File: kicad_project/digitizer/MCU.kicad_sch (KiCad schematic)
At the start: 27 parts, among them J401 SHF-105-01-L-D-TH-TR, U401 ATSAM4E8EA-AN

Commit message: updated schematic to use all 0805 parts (both caps and resistors)
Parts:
- C401, C403, C404, C405, C406, C407, C408, C409, C410, C411, C412, C413, C414, C415, C416: footprint Capacitor_SMD:C_2220_5650Metric_Pad1.97x5.40mm_HandSolder -> Capacitor_SMD:C_0805_2012Metric_Pad1.18x1.45mm_HandSolder
- C402: footprint Capacitor_Tantalum_SMD:CP_EIA-6032-20_AVX-F_Pad2.25x2.35mm_HandSolder -> Capacitor_SMD:C_0805_2012Metric_Pad1.18x1.45mm_HandSolder
- R401, R402, R403, R404, R405, R406, R407: footprint Resistor_SMD:R_2512_6332Metric_Pad1.40x3.35mm_HandSolder -> Resistor_SMD:R_0805_2012Metric_Pad1.20x1.40mm_HandSolder
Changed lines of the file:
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@@
       (effects (font (size 1.27 1.27)) (justify left))
     )
-    (property "Footprint" "Resistor_SMD:R_2512_6332Metric_Pad1.40x3.35mm_HandSolder" (id 2) (at 66.04 90.17 0)
+    (property "Footprint" "Resistor_SMD:R_0805_2012Metric_Pad1.20x1.40mm_HandSolder" (id 2) (at 66.04 90.17 0)
       (effects (font (size 1.27 1.27)) hide)
     )
@@
       (effects (font (size 1.27 1.27)) (justify left))
     )
-    (property "Footprint" "Capacitor_SMD:C_2220_5650Metric_Pad1.97x5.40mm_HandSolder" (id 2) (at 243.84 52.07 0)
+    (property "Footprint" "Capacitor_SMD:C_0805_2012Metric_Pad1.18x1.45mm_HandSolder" (id 2) (at 243.84 52.07 0)
       (effects (font (size 1.27 1.27)) hide)
     )
@@
       (effects (font (size 1.27 1.27)) (justify left))
     )
-    (property "Footprint" "Resistor_SMD:R_2512_6332Metric_Pad1.40x3.35mm_HandSolder" (id 2) (at 49.53 132.08 0)
+    (property "Footprint" "Resistor_SMD:R_0805_2012Metric_Pad1.20x1.40mm_HandSolder" (id 2) (at 49.53 132.08 0)
       (effects (font (size 1.27 1.27)) hide)
     )
@@
       (effects (font (size 1.27 1.27)) (justify left))
     )
-    (property "Footprint" "Resistor_SMD:R_2512_6332Metric_Pad1.40x3.35mm_HandSolder" (id 2) (at 151.13 78.74 0)
+    (property "Footprint" "Resistor_SMD:R_0805_2012Metric_Pad1.20x1.40mm_HandSolder" (id 2) (at 151.13 78.74 0)
       (effects (font (size 1.27 1.27)) hide)
     )
@@
       (effects (font (size 1.27 1.27)) (justify left))
     )
-    (property "Footprint" "Capacitor_SMD:C_2220_5650Metric_Pad1.97x5.40mm_HandSolder" (id 2) (at 238.76 146.05 0)
+    (property "Footprint" "Capacitor_SMD:C_0805_2012Metric_Pad1.18x1.45mm_HandSolder" (id 2) (at 238.76 146.05 0)
       (effects (font (size 1.27 1.27)) hide)
     )
@@
       (effects (font (size 1.27 1.27)) (justify left))
     )
-    (property "Footprint" "Capacitor_SMD:C_2220_5650Metric_Pad1.97x5.40mm_HandSolder" (id 2) (at 246.38 146.05 0)
+    (property "Footprint" "Capacitor_SMD:C_0805_2012Metric_Pad1.18x1.45mm_HandSolder" (id 2) (at 246.38 146.05 0)
       (effects (font (size 1.27 1.27)) hide)
     )
@@
       (effects (font (size 1.27 1.27)) (justify left))
     )
-    (property "Footprint" "Capacitor_Tantalum_SMD:CP_EIA-6032-20_AVX-F_Pad2.25x2.35mm_HandSolder" (id 2) (at 237.49 34.29 0)
+    (property "Footprint" "Capacitor_SMD:C_0805_2012Metric_Pad1.18x1.45mm_HandSolder" (id 2) (at 237.49 34.29 0)
       (effects (font (size 1.27 1.27)) hide)
     )
@@
       (effects (font (size 1.27 1.27)) (justify left))
     )
-    (property "Footprint" "Capacitor_SMD:C_2220_5650Metric_Pad1.97x5.40mm_HandSolder" (id 2) (at 213.36 146.05 0)
+    (property "Footprint" "Capacitor_SMD:C_0805_2012Metric_Pad1.18x1.45mm_HandSolder" (id 2) (at 213.36 146.05 0)
       (effects (font (size 1.27 1.27)) hide)
     )
@@
       (effects (font (size 1.27 1.27)) (justify left))
     )
-    (property "Footprint" "Capacitor_SMD:C_2220_5650Metric_Pad1.97x5.40mm_HandSolder" (id 2) (at 254 146.05 0)
+    (property "Footprint" "Capacitor_SMD:C_0805_2012Metric_Pad1.18x1.45mm_HandSolder" (id 2) (at 254 146.05 0)
       (effects (font (size 1.27 1.27)) hide)
     )
@@
       (effects (font (size 1.27 1.27)) (justify left))
     )
-    (property "Footprint" "Capacitor_SMD:C_2220_5650Metric_Pad1.97x5.40mm_HandSolder" (id 2) (at 62.23 146.05 0)
+    (property "Footprint" "Capacitor_SMD:C_0805_2012Metric_Pad1.18x1.45mm_HandSolder" (id 2) (at 62.23 146.05 0)
       (effects (font (size 1.27 1.27)) hide)
     )
@@
       (effects (font (size 1.27 1.27)) (justify left))
     )
-    (property "Footprint" "Resistor_SMD:R_2512_6332Metric_Pad1.40x3.35mm_HandSolder" (id 2) (at 58.42 74.93 0)
+    (property "Footprint" "Resistor_SMD:R_0805_2012Metric_Pad1.20x1.40mm_HandSolder" (id 2) (at 58.42 74.93 0)
       (effects (font (size 1.27 1.27)) hide)
     )
@@
       (effects (font (size 1.27 1.27)) (justify left))
     )
-    (property "Footprint" "Resistor_SMD:R_2512_6332Metric_Pad1.40x3.35mm_HandSolder" (id 2) (at 62.23 82.55 0)
+    (property "Footprint" "Resistor_SMD:R_0805_2012Metric_Pad1.20x1.40mm_HandSolder" (id 2) (at 62.23 82.55 0)
       (effects (font (size 1.27 1.27)) hide)
     )
@@
       (effects (font (size 1.27 1.27)) (justify left))
     )
-    (property "Footprint" "Capacitor_SMD:C_2220_5650Metric_Pad1.97x5.40mm_HandSolder" (id 2) (at 198.12 146.05 0)
+    (property "Footprint" "Capacitor_SMD:C_0805_2012Metric_Pad1.18x1.45mm_HandSolder" (id 2) (at 198.12 146.05 0)
       (effects (font (size 1.27 1.27)) hide)
     )
@@
       (effects (font (size 1.27 1.27)) (justify left))
     )
-    (property "Footprint" "Capacitor_SMD:C_2220_5650Metric_Pad1.97x5.40mm_HandSolder" (id 2) (at 243.84 34.29 0)
+    (property "Footprint" "Capacitor_SMD:C_0805_2012Metric_Pad1.18x1.45mm_HandSolder" (id 2) (at 243.84 34.29 0)
       (effects (font (size 1.27 1.27)) hide)
     )
@@
       (effects (font (size 1.27 1.27)) (justify left))
     )
-    (property "Footprint" "Capacitor_SMD:C_2220_5650Metric_Pad1.97x5.40mm_HandSolder" (id 2) (at 269.24 146.05 0)
+    (property "Footprint" "Capacitor_SMD:C_0805_2012Metric_Pad1.18x1.45mm_HandSolder" (id 2) (at 269.24 146.05 0)
       (effects (font (size 1.27 1.27)) hide)
     )
@@
       (effects (font (size 1.27 1.27)) (justify left))
     )
-    (property "Footprint" "Capacitor_SMD:C_2220_5650Metric_Pad1.97x5.40mm_HandSolder" (id 2) (at 276.86 146.05 0)
+    (property "Footprint" "Capacitor_SMD:C_0805_2012Metric_Pad1.18x1.45mm_HandSolder" (id 2) (at 276.86 146.05 0)
       (effects (font (size 1.27 1.27)) hide)
     )
@@
       (effects (font (size 1.27 1.27)) (justify left))
     )
-    (property "Footprint" "Capacitor_SMD:C_2220_5650Metric_Pad1.97x5.40mm_HandSolder" (id 2) (at 243.84 21.59 0)
+    (property "Footprint" "Capacitor_SMD:C_0805_2012Metric_Pad1.18x1.45mm_HandSolder" (id 2) (at 243.84 21.59 0)
       (effects (font (size 1.27 1.27)) hide)
     )
@@
       (effects (font (size 1.27 1.27)) (justify left))
     )
-    (property "Footprint" "Capacitor_SMD:C_2220_5650Metric_Pad1.97x5.40mm_HandSolder" (id 2) (at 261.62 146.05 0)
+    (property "Footprint" "Capacitor_SMD:C_0805_2012Metric_Pad1.18x1.45mm_HandSolder" (id 2) (at 261.62 146.05 0)
       (effects (font (size 1.27 1.27)) hide)
     )
@@
       (effects (font (size 1.27 1.27)) (justify left))
     )
-    (property "Footprint" "Capacitor_SMD:C_2220_5650Metric_Pad1.97x5.40mm_HandSolder" (id 2) (at 228.6 146.05 0)
+    (property "Footprint" "Capacitor_SMD:C_0805_2012Metric_Pad1.18x1.45mm_HandSolder" (id 2) (at 228.6 146.05 0)
       (effects (font (size 1.27 1.27)) hide)
     )
@@
       (effects (font (size 1.27 1.27)) (justify left))
     )
-    (property "Footprint" "Capacitor_SMD:C_2220_5650Metric_Pad1.97x5.40mm_HandSolder" (id 2) (at 220.98 146.05 0)
+    (property "Footprint" "Capacitor_SMD:C_0805_2012Metric_Pad1.18x1.45mm_HandSolder" (id 2) (at 220.98 146.05 0)
       (effects (font (size 1.27 1.27)) hide)
     )
@@
       (effects (font (size 1.27 1.27)) (justify left))
     )
-    (property "Footprint" "Resistor_SMD:R_2512_6332Metric_Pad1.40x3.35mm_HandSolder" (id 2) (at 147.32 78.74 0)
+    (property "Footprint" "Resistor_SMD:R_0805_2012Metric_Pad1.20x1.40mm_HandSolder" (id 2) (at 147.32 78.74 0)
       (effects (font (size 1.27 1.27)) hide)
     )
@@
       (effects (font (size 1.27 1.27)) (justify left))
     )
-    (property "Footprint" "Capacitor_SMD:C_2220_5650Metric_Pad1.97x5.40mm_HandSolder" (id 2) (at 205.74 146.05 0)
+    (property "Footprint" "Capacitor_SMD:C_0805_2012Metric_Pad1.18x1.45mm_HandSolder" (id 2) (at 205.74 146.05 0)
       (effects (font (size 1.27 1.27)) hide)
     )
@@
       (effects (font (size 1.27 1.27)) (justify left))
     )
-    (property "Footprint" "Resistor_SMD:R_2512_6332Metric_Pad1.40x3.35mm_HandSolder" (id 2) (at 54.61 68.58 0)
-      (effects (font (size 1.27 1.27)) hide)
-    )
+    (property "Footprint" "Resistor_SMD:R_0805_2012Metric_Pad1.20x1.40mm_HandSolder" (id 2) (at 54.61 68.58 0)
+      (effects (font (size 1.27 1.27)) hide)
+    )

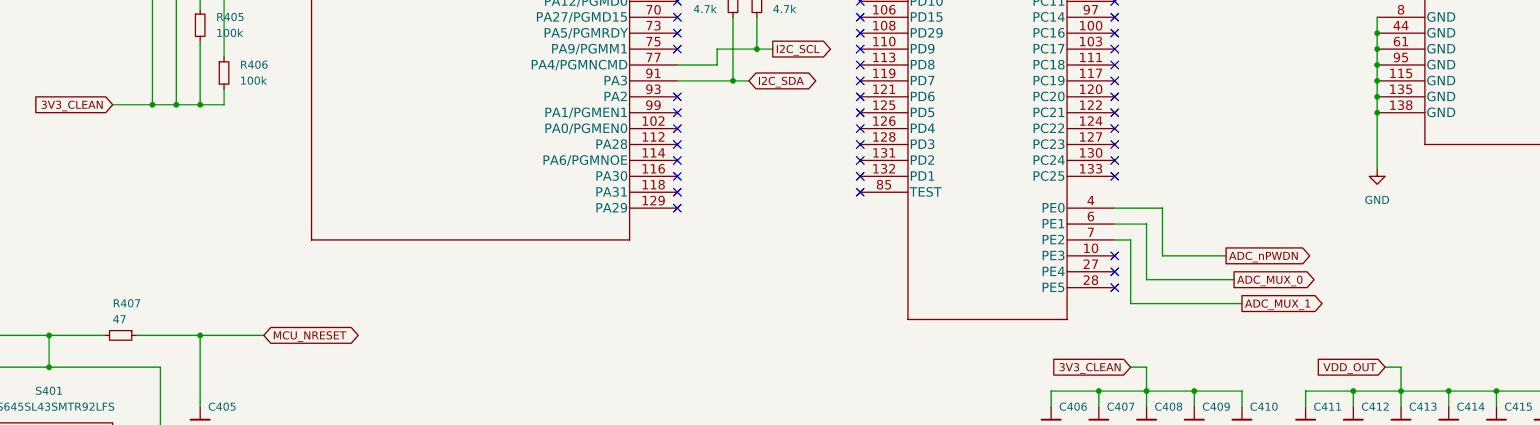
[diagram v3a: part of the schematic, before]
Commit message: added some 0R resistors to pads to allow for easier board modding
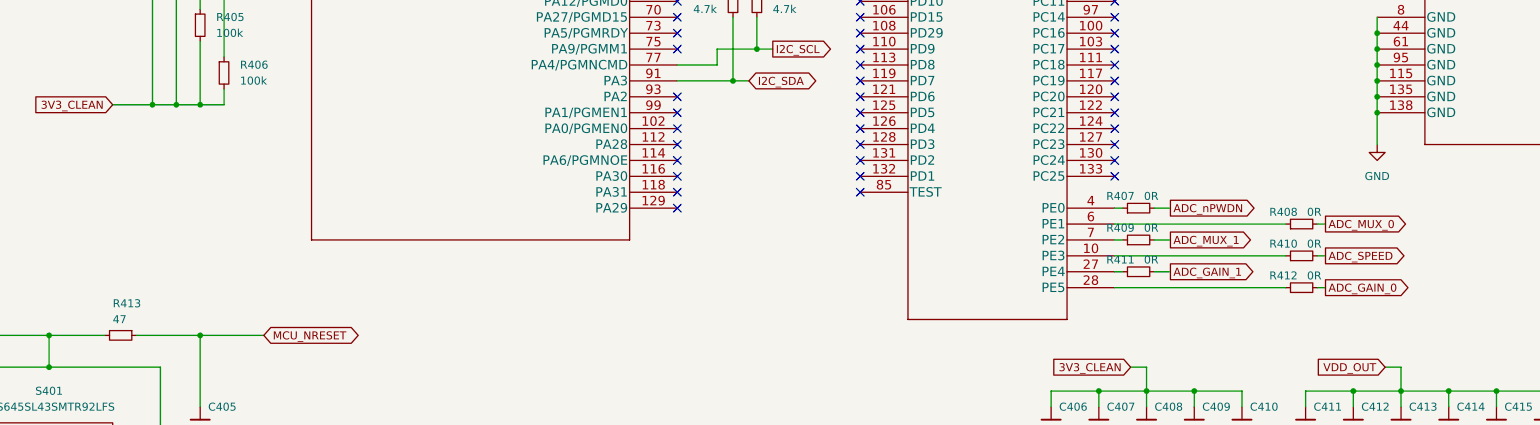
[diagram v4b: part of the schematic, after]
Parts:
- added R407, R408, R409, R410, R411, R412: 0R, Resistor_SMD:R_0805_2012Metric_Pad1.20x1.40mm_HandSolder, symbol Device:R_Small
- renumbered R407 to R413
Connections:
- net ADC_MUX_0: now also R408.2; no longer U401.6 (PE1)
- net ADC_MUX_1: now also R409.2; no longer U401.7 (PE2)
- net ADC_nPWDN: now also R407.2; no longer U401.4 (PE0)
- net at U401.10 (PE3): now also R410.1
- net at U401.27 (PE4): now also R411.1
- net at U401.28 (PE5): now also R412.1
- new net: R407.1, U401.4 (PE0)
- new net: R408.1, U401.6 (PE1)
- new net: R409.1, U401.7 (PE2)
- new net ADC_GAIN_0: R412.2
- new net ADC_GAIN_1: R411.2
- new net ADC_SPEED: R410.2
- no-connect marks 107 -> 104

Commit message: fixed everything up
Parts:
- removed R407, R408, R409, R410, R411, R412: 0R, Resistor_SMD:R_0805_2012Metric_Pad1.20x1.40mm_HandSolder, symbol Device:R_Small
- renumbered R413 to R407
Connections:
- net ADC_GAIN_0: now also U401.28 (PE5)
- net ADC_GAIN_1: now also U401.27 (PE4)
- net ADC_MUX_0: now also U401.6 (PE1)
- net ADC_MUX_1: now also U401.7 (PE2)
- net ADC_SPEED: now also U401.10 (PE3)
- net ADC_nPWDN: now also U401.4 (PE0)
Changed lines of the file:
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@@
     (stroke (width 0) (type default) (color 0 0 0 0))
   )
-  (wire (pts (xy 240.665 119.38) (xy 241.935 119.38))
-    (stroke (width 0) (type default) (color 0 0 0 0))
-  )
-  (wire (pts (xy 214.63 121.92) (xy 217.17 121.92))
+  (wire (pts (xy 208.28 121.92) (xy 217.17 121.92))
     (stroke (width 0) (type default) (color 0 0 0 0))
   )
@@
     (stroke (width 0) (type default) (color 0 0 0 0))
   )
-  (wire (pts (xy 209.55 116.84) (xy 208.28 116.84))
+  (wire (pts (xy 208.28 116.84) (xy 217.17 116.84))
     (stroke (width 0) (type default) (color 0 0 0 0))
   )
@@
     (stroke (width 0) (type default) (color 0 0 0 0))
   )
-  (wire (pts (xy 214.63 116.84) (xy 217.17 116.84))
-    (stroke (width 0) (type default) (color 0 0 0 0))
-  )
   (wire (pts (xy 243.84 38.1) (xy 243.84 39.37))
     (stroke (width 0) (type default) (color 0 0 0 0))
@@
     (stroke (width 0) (type default) (color 0 0 0 0))
   )
-  (wire (pts (xy 240.665 114.3) (xy 241.935 114.3))
-    (stroke (width 0) (type default) (color 0 0 0 0))
-  )
   (wire (pts (xy 237.49 30.48) (xy 237.49 31.75))
     (stroke (width 0) (type default) (color 0 0 0 0))
@@
     (stroke (width 0) (type default) (color 0 0 0 0))
   )
-  (wire (pts (xy 209.55 111.76) (xy 208.28 111.76))
-    (stroke (width 0) (type default) (color 0 0 0 0))
-  )
   (wire (pts (xy 246.38 140.97) (xy 246.38 143.51))
     (stroke (width 0) (type default) (color 0 0 0 0))
@@
     (stroke (width 0) (type default) (color 0 0 0 0))
   )
-  (wire (pts (xy 208.28 119.38) (xy 235.585 119.38))
+  (wire (pts (xy 208.28 119.38) (xy 241.935 119.38))
     (stroke (width 0) (type default) (color 0 0 0 0))
   )
@@
     (stroke (width 0) (type default) (color 0 0 0 0))
   )
-  (wire (pts (xy 208.28 114.3) (xy 235.585 114.3))
+  (wire (pts (xy 208.28 114.3) (xy 241.935 114.3))
     (stroke (width 0) (type default) (color 0 0 0 0))
   )
@@
     (stroke (width 0) (type default) (color 0 0 0 0))
   )
-  (wire (pts (xy 240.665 124.46) (xy 241.935 124.46))
-    (stroke (width 0) (type default) (color 0 0 0 0))
-  )
   (wire (pts (xy 243.84 30.48) (xy 250.19 30.48))
     (stroke (width 0) (type default) (color 0 0 0 0))
@@
     (stroke (width 0) (type default) (color 0 0 0 0))
   )
-  (wire (pts (xy 208.28 121.92) (xy 209.55 121.92))
-    (stroke (width 0) (type default) (color 0 0 0 0))
-  )
   (wire (pts (xy 151.13 73.66) (xy 151.13 76.2))
     (stroke (width 0) (type default) (color 0 0 0 0))
@@
     (stroke (width 0) (type default) (color 0 0 0 0))
   )
-  (wire (pts (xy 208.28 124.46) (xy 235.585 124.46))
+  (wire (pts (xy 208.28 124.46) (xy 241.935 124.46))
     (stroke (width 0) (type default) (color 0 0 0 0))
   )
@@
     (stroke (width 0) (type default) (color 0 0 0 0))
   )
-  (wire (pts (xy 214.63 111.76) (xy 217.17 111.76))
+  (wire (pts (xy 208.28 111.76) (xy 217.17 111.76))
     (stroke (width 0) (type default) (color 0 0 0 0))
   )
@@
     )
     (pin "1")
-  )
-  (symbol (lib_id "Device:R_Small") (at 212.09 121.92 90) (unit 1)
-    (in_bom yes) (on_board yes)
-    (property "Reference" "R411" (id 0) (at 211.455 120.015 90)
-      (effects (font (size 1.27 1.27)) (justify left))
-    )
-    (property "Value" "0R" (id 1) (at 215.265 120.015 90)
-      (effects (font (size 1.27 1.27)) (justify left))
-    )
-    (property "Footprint" "Resistor_SMD:R_0805_2012Metric_Pad1.20x1.40mm_HandSolder" (id 2) (at 212.09 121.92 0)
-      (effects (font (size 1.27 1.27)) hide)
-    )
-    (property "Datasheet" "~" (id 3) (at 212.09 121.92 0)
-      (effects (font (size 1.27 1.27)) hide)
-    )
-    (pin "1")
-    (pin "2")
-  )
-  (symbol (lib_id "Device:R_Small") (at 212.09 111.76 90) (unit 1)
-    (in_bom yes) (on_board yes)
-    (property "Reference" "R407" (id 0) (at 211.455 109.855 90)
-      (effects (font (size 1.27 1.27)) (justify left))
-    )
-    (property "Value" "0R" (id 1) (at 215.265 109.855 90)
-      (effects (font (size 1.27 1.27)) (justify left))
-    )
-    (property "Footprint" "Resistor_SMD:R_0805_2012Metric_Pad1.20x1.40mm_HandSolder" (id 2) (at 212.09 111.76 0)
-      (effects (font (size 1.27 1.27)) hide)
-    )
-    (property "Datasheet" "~" (id 3) (at 212.09 111.76 0)
-      (effects (font (size 1.27 1.27)) hide)
-    )
-    (pin "1")
-    (pin "2")
   )
   (symbol (lib_id "Device:R_Small") (at 66.04 90.17 0) (unit 1)
@@
     (pin "2")
   )
-  (symbol (lib_id "Device:R_Small") (at 238.125 124.46 90) (unit 1)
-    (in_bom yes) (on_board yes)
-    (property "Reference" "R412" (id 0) (at 237.49 122.555 90)
-      (effects (font (size 1.27 1.27)) (justify left))
-    )
-    (property "Value" "0R" (id 1) (at 241.3 122.555 90)
-      (effects (font (size 1.27 1.27)) (justify left))
-    )
-    (property "Footprint" "Resistor_SMD:R_0805_2012Metric_Pad1.20x1.40mm_HandSolder" (id 2) (at 238.125 124.46 0)
-      (effects (font (size 1.27 1.27)) hide)
-    )
-    (property "Datasheet" "~" (id 3) (at 238.125 124.46 0)
-      (effects (font (size 1.27 1.27)) hide)
-    )
-    (pin "1")
-    (pin "2")
-  )
   (symbol (lib_id "Device:R_Small") (at 49.53 132.08 270) (unit 1)
     (in_bom yes) (on_board yes)
-    (property "Reference" "R413" (id 0) (at 48.26 127 90)
+    (property "Reference" "R407" (id 0) (at 48.26 127 90)
       (effects (font (size 1.27 1.27)) (justify left))
     )
@@
     )
     (property "Datasheet" "~" (id 3) (at 238.76 146.05 0)
-      (effects (font (size 1.27 1.27)) hide)
-    )
-    (pin "1")
-    (pin "2")
-  )
-  (symbol (lib_id "Device:R_Small") (at 212.09 116.84 90) (unit 1)
-    (in_bom yes) (on_board yes)
-    (property "Reference" "R409" (id 0) (at 211.455 114.935 90)
-      (effects (font (size 1.27 1.27)) (justify left))
-    )
-    (property "Value" "0R" (id 1) (at 215.265 114.935 90)
-      (effects (font (size 1.27 1.27)) (justify left))
-    )
-    (property "Footprint" "Resistor_SMD:R_0805_2012Metric_Pad1.20x1.40mm_HandSolder" (id 2) (at 212.09 116.84 0)
-      (effects (font (size 1.27 1.27)) hide)
-    )
-    (property "Datasheet" "~" (id 3) (at 212.09 116.84 0)
       (effects (font (size 1.27 1.27)) hide)
     )
@@
     (pin "2")
   )
-  (symbol (lib_id "Device:R_Small") (at 238.125 114.3 90) (unit 1)
-    (in_bom yes) (on_board yes)
-    (property "Reference" "R408" (id 0) (at 237.49 112.395 90)
-      (effects (font (size 1.27 1.27)) (justify left))
-    )
-    (property "Value" "0R" (id 1) (at 241.3 112.395 90)
-      (effects (font (size 1.27 1.27)) (justify left))
-    )
-    (property "Footprint" "Resistor_SMD:R_0805_2012Metric_Pad1.20x1.40mm_HandSolder" (id 2) (at 238.125 114.3 0)
-      (effects (font (size 1.27 1.27)) hide)
-    )
-    (property "Datasheet" "~" (id 3) (at 238.125 114.3 0)
-      (effects (font (size 1.27 1.27)) hide)
-    )
-    (pin "1")
-    (pin "2")
-  )
   (symbol (lib_id "Device:L_Small") (at 238.76 19.05 90) (unit 1)
     (in_bom yes) (on_board yes)
@@
       (effects (font (size 1.27 1.27)) hide)
     )
-    (pin "1")
-    (pin "2")
-  )
-  (symbol (lib_id "Device:R_Small") (at 238.125 119.38 90) (unit 1)
-    (in_bom yes) (on_board yes)
-    (property "Reference" "R410" (id 0) (at 237.49 117.475 90)
-      (effects (font (size 1.27 1.27)) (justify left))
-    )
-    (property "Value" "0R" (id 1) (at 241.3 117.475 90)
-      (effects (font (size 1.27 1.27)) (justify left))
-    )
-    (property "Footprint" "Resistor_SMD:R_0805_2012Metric_Pad1.20x1.40mm_HandSolder" (id 2) (at 238.125 119.38 0)
-      (effects (font (size 1.27 1.27)) hide)
-    )
-    (property "Datasheet" "~" (id 3) (at 238.125 119.38 0)
-      (effects (font (size 1.27 1.27)) hide)
-    )
